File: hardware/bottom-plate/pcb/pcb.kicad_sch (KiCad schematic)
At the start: 27 parts, among them U1 Pico

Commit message: bottom plate schematic, and removed some random stuff
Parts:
- removed DMUX1: TCA9555PWR, Package_SO:TSSOP-24_4.4x7.8mm_P0.65mm, symbol Interface_Expansion:TCA9535PWR
- removed KICK_PWR1: XT30-F, Connector_AMASS:AMASS_XT30U-F_1x02_P5.0mm_Vertical, symbol Connector_Generic:Conn_01x02
- removed PWR1: XT60-M, Connector_AMASS:AMASS_XT60-M_1x02_P7.20mm_Vertical, symbol Connector_Generic:Conn_01x02
- added CTRL1, LOADCELL1: Conn_01x04, Connector_JST:JST_XH_B4B-XH-A_1x04_P2.50mm_Vertical, symbol Connector_Generic:Conn_01x04
- added DMUX1, DMUX2: MCP23S17_SO, Package_SO:SOIC-28W_7.5x17.9mm_P1.27mm, symbol Interface_Expansion:MCP23S17_SO
- added J1: Conn_01x03, symbol Connector_Generic:Conn_01x03
- added KICK1: Conn_01x03, Connector_JST:JST_XH_B3B-XH-A_1x03_P2.50mm_Vertical, symbol Connector_Generic:Conn_01x03
- added R59: 2.7K, PCM_Resistor_SMD_AKL:R_0603_1608Metric_Pad0.98x0.95mm_HandSolder, symbol Device:R
- added R62, R63, R65: DNP, PCM_Resistor_SMD_AKL:R_0603_1608Metric_Pad0.98x0.95mm_HandSolder, symbol Device:R
- added R64, R66: 0R, PCM_Resistor_SMD_AKL:R_0603_1608Metric_Pad0.98x0.95mm_HandSolder, symbol Device:R
- ADC1, ADC2: footprint Package_SO:VSSOP-10_3x3mm_P0.5mm -> Package_SO:TSSOP-10_3x3mm_P0.5mm
- R60: value 4.7K -> 2.7K
- R61: value 4.7K -> 0R
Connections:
- net ADC2_AIN1 is gone; now on net DRV5_IPROPI: ADC2.5 (AIN1)
- net +3V3: now also DMUX1.9 (VDD), DMUX2.9 (VDD), J1.3 (Pin_3), LOADCELL1.1 (Pin_1), R59.1, R63.2, R65.2; no longer U1.36 (3V3)
- net ADC_INT1: now also DMUX1.1 (GPB0)
- net ADC_INT2: now also DMUX1.2 (GPB1)
- net DRV1_NFAULT: now also DMUX1.5 (GPB4)
- net DRV1_NSLEEP: now also DMUX2.2 (GPB1)
- net DRV1_OFF: now also DMUX2.1 (GPB0)
- net DRV1_SCS: now also DMUX2.23 (GPA2); no longer U1.21 (GPIO16)
- net DRV2_NFAULT: now also DMUX1.6 (GPB5)
- net DRV2_NSLEEP: now also DMUX2.4 (GPB3)
- net DRV2_OFF: now also DMUX2.3 (GPB2)
- net DRV2_SCS: now also DMUX2.24 (GPA3)
- net DRV3_NFAULT: now also DMUX1.7 (GPB6)
- net DRV3_NSLEEP: now also DMUX2.6 (GPB5)
- net DRV3_OFF: now also DMUX2.5 (GPB4)
- net DRV3_SCS: now also DMUX2.25 (GPA4)
- net DRV4_NFAULT: now also DMUX1.8 (GPB7)
- net DRV4_NSLEEP: now also DMUX2.8 (GPB7)
- net DRV4_OFF: now also DMUX2.7 (GPB6)
- net DRV4_SCS: now also DMUX2.26 (GPA5)
- net DRV5_IN1: now also U1.19 (GPIO14); no longer U1.25 (GPIO19)
- net DRV5_IN2: now also U1.20 (GPIO15); no longer U1.24 (GPIO18)
- net DRV5_IPROPI: no longer ADC1.7 (AIN3)
- net DRV5_NFAULT: now also DMUX1.21 (GPA0)
- net DRV5_NSLEEP: now also DMUX2.22 (GPA1)
- net DRV5_OFF: now also DMUX2.21 (GPA0)
- net DRV5_SCS: now also DMUX2.27 (GPA6)
- net GND: now also DMUX1.10 (VSS), DMUX2.10 (VSS), J1.2 (Pin_2), KICK1.1 (Pin_1), LOADCELL1.4 (Pin_4), R62.2, R64.1, R66.1
- net LOADCELL_A+: now also LOADCELL1.2 (Pin_2)
- net LOADCELL_A-: now also LOADCELL1.3 (Pin_3)
- net MOUSE1_MOT: now also DMUX1.3 (GPB2)
- net MOUSE1_RST: now also DMUX1.23 (GPA2)
- net MOUSE2_MOT: now also DMUX1.4 (GPB3)
- net MOUSE2_RST: now also DMUX1.24 (GPA3)
- net MUX_S0: now also DMUX1.25 (GPA4); no longer U1.19 (GPIO14)
- net MUX_S1: now also DMUX1.26 (GPA5); no longer U1.20 (GPIO15)
- net MUX_S2: now also DMUX1.27 (GPA6); no longer U1.27 (GPIO21)
- net MUX_S3: now also DMUX1.28 (GPA7); no longer U1.26 (GPIO20)
- net RUN: now also CTRL1.1 (Pin_1)
- net EN: now reaches U1.37 (3V3_EN)
- net EN: now also CTRL1.2 (Pin_2)
- net +5V: now reaches U1.39 (VSYS)
- net at R53.1, R54.2: now also DMUX1.15 (A0)
- net at R55.1, R56.2: now also DMUX1.16 (A1)
- net at R57.1, R58.2: now also DMUX1.17 (A2)
- net +12V renamed VCC
- net VCC: now also KICK1.2 (Pin_2)
- net DMUX_INT renamed RX0
- net RX0: now also CTRL1.3 (Pin_3)
- net MISO renamed SPI0.MISO
- net SPI0.MISO: now also DMUX1.14 (SO), DMUX2.14 (SO)
- net MOSI renamed SPI0.MOSI
- net SPI0.MOSI: now also DMUX1.13 (SI), DMUX2.13 (SI)
- net MUX1_COM renamed AMUX1_COM
- net MUX2_COM renamed AMUX2_COM
- net MUX3_COM renamed AMUX3_COM
- net SCL renamed I2C0.SCL
- net I2C0.SCL: now also R60.2; no longer R61.2
- net SCLK renamed SPI0.SCLK
- net SPI0.SCLK: now also DMUX1.12 (SCK), DMUX2.12 (SCK)
- net SDA renamed I2C0.SDA
- net I2C0.SDA: now also R59.2; no longer R60.2
- new net: DMUX2.17 (A2), R65.1, R66.2
- new net: DMUX2.16 (A1), R63.1, R64.2
- new net: DMUX2.15 (A0), R61.2, R62.1
- new net AMUX_EN: DMUX2.28 (GPA7)
- new net DMUX1_INT: DMUX1.20 (INTA), U1.25 (GPIO19)
- new net DMUX2_INT: DMUX1.22 (GPA1), DMUX2.20 (INTA)
- new net DMUX_RESET: DMUX1.18 (~{RESET}), DMUX2.18 (~{RESET}), U1.26 (GPIO20)
- new net DMUX_SCS: DMUX1.11 (~{CS}), DMUX2.11 (~{CS}), U1.27 (GPIO21)
- new net GATE: ADC1.7 (AIN3), J1.1 (Pin_1)
- new net KICK: KICK1.3 (Pin_3), U1.24 (GPIO18)
- new net TX0: CTRL1.4 (Pin_4), U1.21 (GPIO16)
- no-connect marks 22 -> 29
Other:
- added sheet power (power.kicad_sch)
- note added: "SPI address: 0b0100000"
- note added: "SPI address: 0b0100001"
- note added: "pullup resistors for I2C. Adjust values accordingly. 2.7K is probably safe. lower values can be used if capacitance is too high (shouldnt be the case though since its only on board)"
- note removed: "an xt30 has sufficient current for this. but no point (since batt has xt60 as well.)"
- note removed: "pullup resistors for I2C. Adjust values accordingly. 4.7K is probably a safe value."
- note removed: "this might be headers instead. depends on how kicker PCB is mounted"
- moved on the sheet: DRV1, DRV2, DRV3, DRV4, DRV5, MOUSE_FPC1, MOUSE_FPC2, R53, R54, R55, R56, R57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

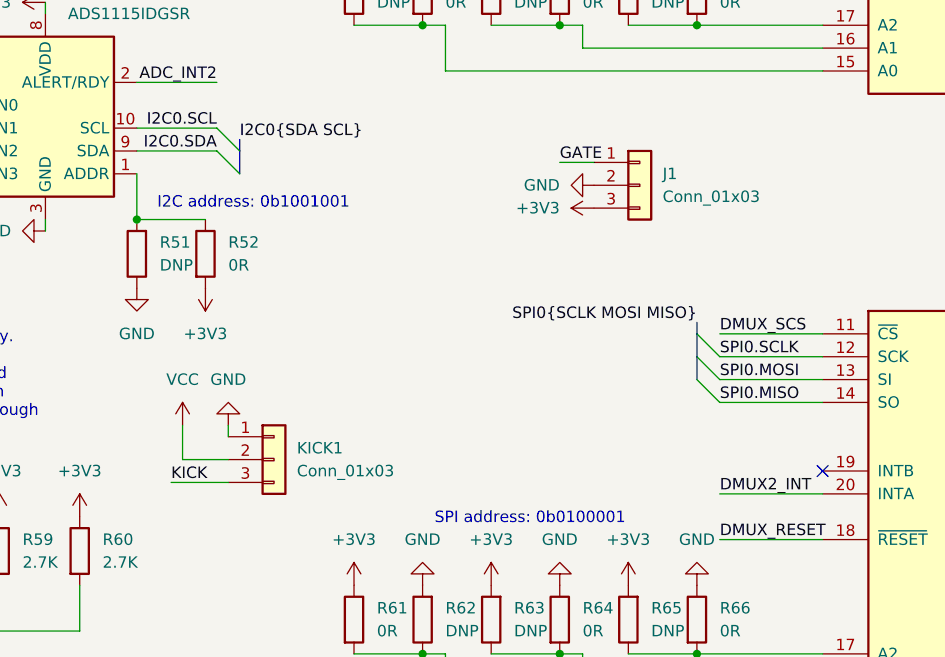
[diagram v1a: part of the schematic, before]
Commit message: kicker pcb done, working on bottom plate
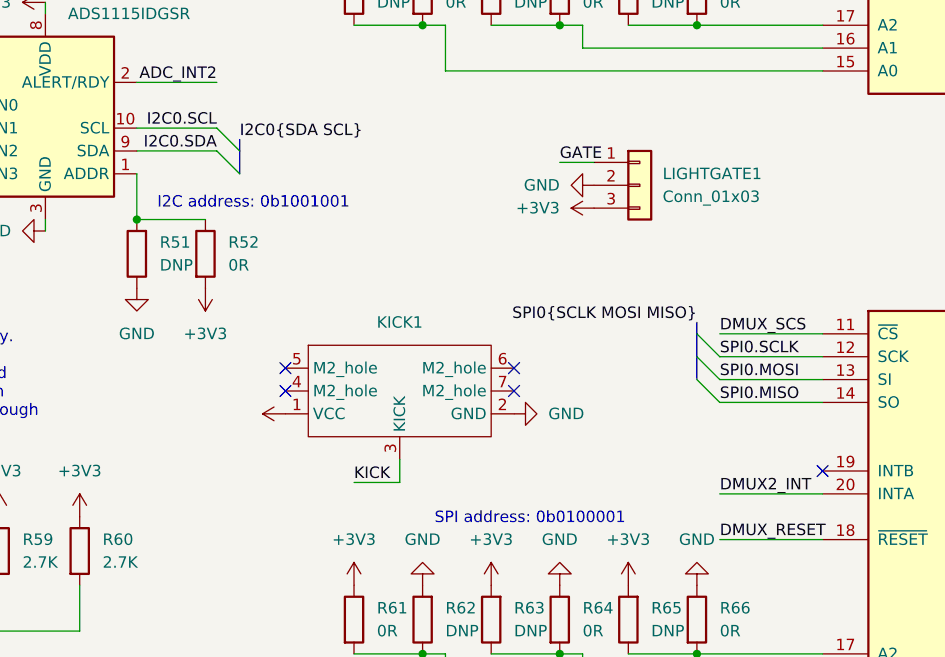
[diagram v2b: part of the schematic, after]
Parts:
- removed KICK1: Conn_01x03, Connector_JST:JST_XH_B3B-XH-A_1x03_P2.50mm_Vertical, symbol Connector_Generic:Conn_01x03
- added KICK1: ~, custom:kicker, symbol custom:kicker
- LIGHTGATE1: renamed from J1; footprint (none) -> Connector_JST:JST_XH_B3B-XH-A_1x03_P2.50mm_Vertical
- R49, R50, R51, R52, R53, R54, R55, R56, R57, R58, R59, R60, R61, R62, R63, R64, R65, R66: footprint PCM_Resistor_SMD_AKL:R_0603_1608Metric_Pad0.98x0.95mm_HandSolder -> PCM_Resistor_SMD_AKL:R_0805_2012Metric_Pad1.15x1.40mm_HandSolder
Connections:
- net GND: now also KICK1.2 (GND)
- net KICK: now also KICK1.3 (KICK)
- net VCC: now also KICK1.1 (VCC)
- no-connect marks 29 -> 33

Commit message: cleaned up bottom plate schematic and added explanations of design decisions. Please read.
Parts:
- added BUCK1: ~, custom:mini560, symbol custom:mini360/560
- added C1: 150uF, Capacitor_SMD:CP_Elec_6.3x7.7, symbol Device:C
- added C2: 1uF, PCM_Capacitor_SMD_AKL:C_0805_2012Metric_Pad1.15x1.40mm_HandSolder, symbol Device:C
- added C3: 22uF, PCM_Capacitor_SMD_AKL:C_0805_2012Metric_Pad1.15x1.40mm_HandSolder, symbol Device:C
- added C4: 10uF, PCM_Capacitor_SMD_AKL:C_0805_2012Metric_Pad1.15x1.40mm_HandSolder, symbol Device:C
- added GATE_LED1: Conn_01x02, Connector_JST:JST_XH_B2B-XH-A_1x02_P2.50mm_Vertical, symbol Connector_Generic:Conn_01x02
- added LDO1: TLV1117-33, Package_TO_SOT_SMD:SOT-223-3_TabPin2, symbol Regulator_Linear:TLV1117-33
- added PWR1: XT60-M, Connector_AMASS:AMASS_XT60-M_1x02_P7.20mm_Vertical, symbol Connector_Generic:Conn_01x02
- added PWR2: XT30-F, Connector_AMASS:AMASS_XT30U-F_1x02_P5.0mm_Vertical, symbol Connector_Generic:Conn_01x02
- U1: footprint RP-Pico Libraries:RPi_Pico_SMD_TH -> RP-Pico Libraries:RPi_Pico_SMD_TH_USBC_cable_cutout
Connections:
- net +3V3: now also C4.2, LDO1.2 (VO)
- net +5V: now also BUCK1.3 (OUT+), C2.2, GATE_LED1.1 (Pin_1), LDO1.3 (VI)
- net ADC_INT1: now also DMUX2.6 (GPB5); no longer DMUX1.1 (GPB0)
- net ADC_INT2: now also DMUX2.7 (GPB6); no longer DMUX1.2 (GPB1)
- net DMUX2_INT: now also DMUX2.8 (GPB7); no longer DMUX1.22 (GPA1)
- net DRV1_NFAULT: now also DMUX2.1 (GPB0); no longer DMUX1.5 (GPB4)
- net DRV1_NSLEEP: now also DMUX1.2 (GPB1); no longer DMUX2.2 (GPB1)
- net DRV1_OFF: now also DMUX1.1 (GPB0); no longer DMUX2.1 (GPB0)
- net DRV1_SCS: now also DMUX2.21 (GPA0); no longer DMUX2.23 (GPA2)
- net DRV2_NFAULT: now also DMUX2.2 (GPB1); no longer DMUX1.6 (GPB5)
- net DRV2_NSLEEP: now also DMUX1.4 (GPB3); no longer DMUX2.4 (GPB3)
- net DRV2_OFF: now also DMUX1.3 (GPB2); no longer DMUX2.3 (GPB2)
- net DRV2_SCS: now also DMUX2.22 (GPA1); no longer DMUX2.24 (GPA3)
- net DRV3_NFAULT: now also DMUX2.3 (GPB2); no longer DMUX1.7 (GPB6)
- net DRV3_NSLEEP: now also DMUX1.6 (GPB5); no longer DMUX2.6 (GPB5)
- net DRV3_OFF: now also DMUX1.5 (GPB4); no longer DMUX2.5 (GPB4)
- net DRV3_SCS: now also DMUX2.23 (GPA2); no longer DMUX2.25 (GPA4)
- net DRV4_NFAULT: now also DMUX2.4 (GPB3); no longer DMUX1.8 (GPB7)
- net DRV4_NSLEEP: now also DMUX1.8 (GPB7); no longer DMUX2.8 (GPB7)
- net DRV4_OFF: now also DMUX1.7 (GPB6); no longer DMUX2.7 (GPB6)
- net DRV4_SCS: now also DMUX2.24 (GPA3); no longer DMUX2.26 (GPA5)
- net DRV5_NFAULT: now also DMUX2.5 (GPB4); no longer DMUX1.21 (GPA0)
- net DRV5_NSLEEP: now also DMUX2.27 (GPA6); no longer DMUX2.22 (GPA1)
- net DRV5_OFF: now also DMUX2.26 (GPA5); no longer DMUX2.21 (GPA0)
- net DRV5_SCS: now also DMUX2.25 (GPA4); no longer DMUX2.27 (GPA6)
- net GND: now also BUCK1.2 (IN-), BUCK1.4 (OUT-), C1.1, C3.1, GATE_LED1.2 (Pin_2), LDO1.1 (GND), PWR1.1 (Pin_1), PWR2.1 (Pin_1)
- net MOUSE1_MOT: now also U1.29 (GPIO22); no longer DMUX1.3 (GPB2)
- net MOUSE1_SCS: now also DMUX1.21 (GPA0); no longer U1.29 (GPIO22)
- net MOUSE2_MOT: now also U1.7 (GPIO5); no longer DMUX1.4 (GPB3)
- net MOUSE2_SCS: now also DMUX1.22 (GPA1); no longer U1.7 (GPIO5)
- net VCC: now also BUCK1.1 (IN+), C1.2, PWR1.2 (Pin_2), PWR2.2 (Pin_2)
- net MUX_S0 renamed AMUX_S0
- net MUX_S1 renamed AMUX_S1
- net MUX_S2 renamed AMUX_S2
- net MUX_S3 renamed AMUX_S3
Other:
- removed sheet line sensors
- removed sheet power
- added sheet line sensor array 1 (line-sensor-array.kicad_sch)
- added sheet line sensor array 2 (line-sensor-array.kicad_sch)
- added sheet line sensor array 3 (line-sensor-array.kicad_sch)
- note added: "16 per array through an analog multiplexer. 48 in total. ALS-PT19 ambient light sensors with HL-PSC-2012H233W(6000-7000K) LEDs shared decoder selection pins, to 3 channels on RP2040"
- note added: "A Pico is used for interfacing the bottom hardware. Connects via UART and USB to the main controller. Pico used for reliable performance and simple implementation with minimal quirks. A USB type-C pico will be preferably used as I hate microusb. Footprint should work fine with both though."
- note added: "ADCs"
- note added: "DRV8244 motor driver breakouts. Output is an XT30. Configured through SPI. Driven via PWM through IN1 and IN2. Current can be read using IPROPI. Read datasheet for more details. DRV5 is for dribbler. A BE-3561 or another brushed motor will be used."
- note added: "Input power smoothing. 150uF should critically damp enough inductance."
- note added: "Lightgate to know if ball is in ball-capture zone. Use of wires to allow different mounting."
- note added: "Loadcell sensor. Can be used in mounting of dribbler suspension to know how well ball is contacting the dribbler. If not using a loadcell, can be used for other analog applications."
- note added: "MINI560 reg, to have a (mostly) guarenteed-to-work and replacable-if-fried design. 5A is way overkill, but the 3A ones are quite sketchy."
- note added: "PMW3360 mouse sensor breakouts, self designed. Uses 1mm pitch FFC connectors. FFC connectors are under this plate for shielding and convenience. 1.6mm thick breakouts has a bit too little ground clearance. Still workable though."
- note added: "Power to middle (and then top) plate. Why not splice wires? It's messy and I don't want to."
- note added: "Reading some sensors, plus monitoring motor currents. Lightgate and loadcell should be on seperate ADCs to minimise contention (especially of the interrupt). Motor currents need not be monitored, but would be cool. Loadcell might not be used due to mass limitations."
- note added: "So the rest of the design can be simpler. And there is only one UART channel on Pi, so only one low-latency microcontroller can exist, unless UART addressing is used, which adds overhead and shares the already limited bandwidth due to running close to many rapidly switching currents. Also, to take up as much bottom real estate as possible, so things don't need to block the camera. And also becaus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"
- note added: "UART channel for low-bandwidth, highly latency sensitive communication between bottom plate and main controller. Also as a backup if USB latencies somehow end up being too high, The bottom plate is more latency sensitive due to it controlling all the movements of the bot."
- note added: "Why so many? Because I don't want to hardwire most configuration pins / have them be set by a jumper. And that there aren't nearly enough pins on the pico. Interrupts also run through here, as there are insuffient pins on the pico. A second microcontroller can be used, but adds unnecessary software complexity when digital multiplexers work fine. 10MHz SPI digital multiplexers are used to be fast 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"
- note added: "an xt30 has sufficient current for this. but no point (since batt has xt60 as well.)"
- note added: "control"
- note added: "digital multiplexers"
- note added: "kicker"
- note added: "line sensor arrays"
- note added: "motor drivers"
- note added: "mouse sensors"
- note added: "pullup resistors for I2C. Internal pullups of the RP2040 might be too weak to reliably drive 400kHz I2C. Adjust values accordingly, 2.7K is probably safe. lower values can be used if capacitance is too high. And of course, no running I2C on wires."
- note added: "why so much stuff on the bottom plate?"
- note removed: "pullup resistors for I2C. Adjust values accordingly. 2.7K is probably safe. lower values can be used if capacitance is too high (shouldnt be the case though since its only on board)"
- moved on the sheet: ADC1, ADC2, CTRL1, DMUX1, DMUX2, DRV1, DRV2, DRV3, DRV4, DRV5, KICK1, LIGHTGATE1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

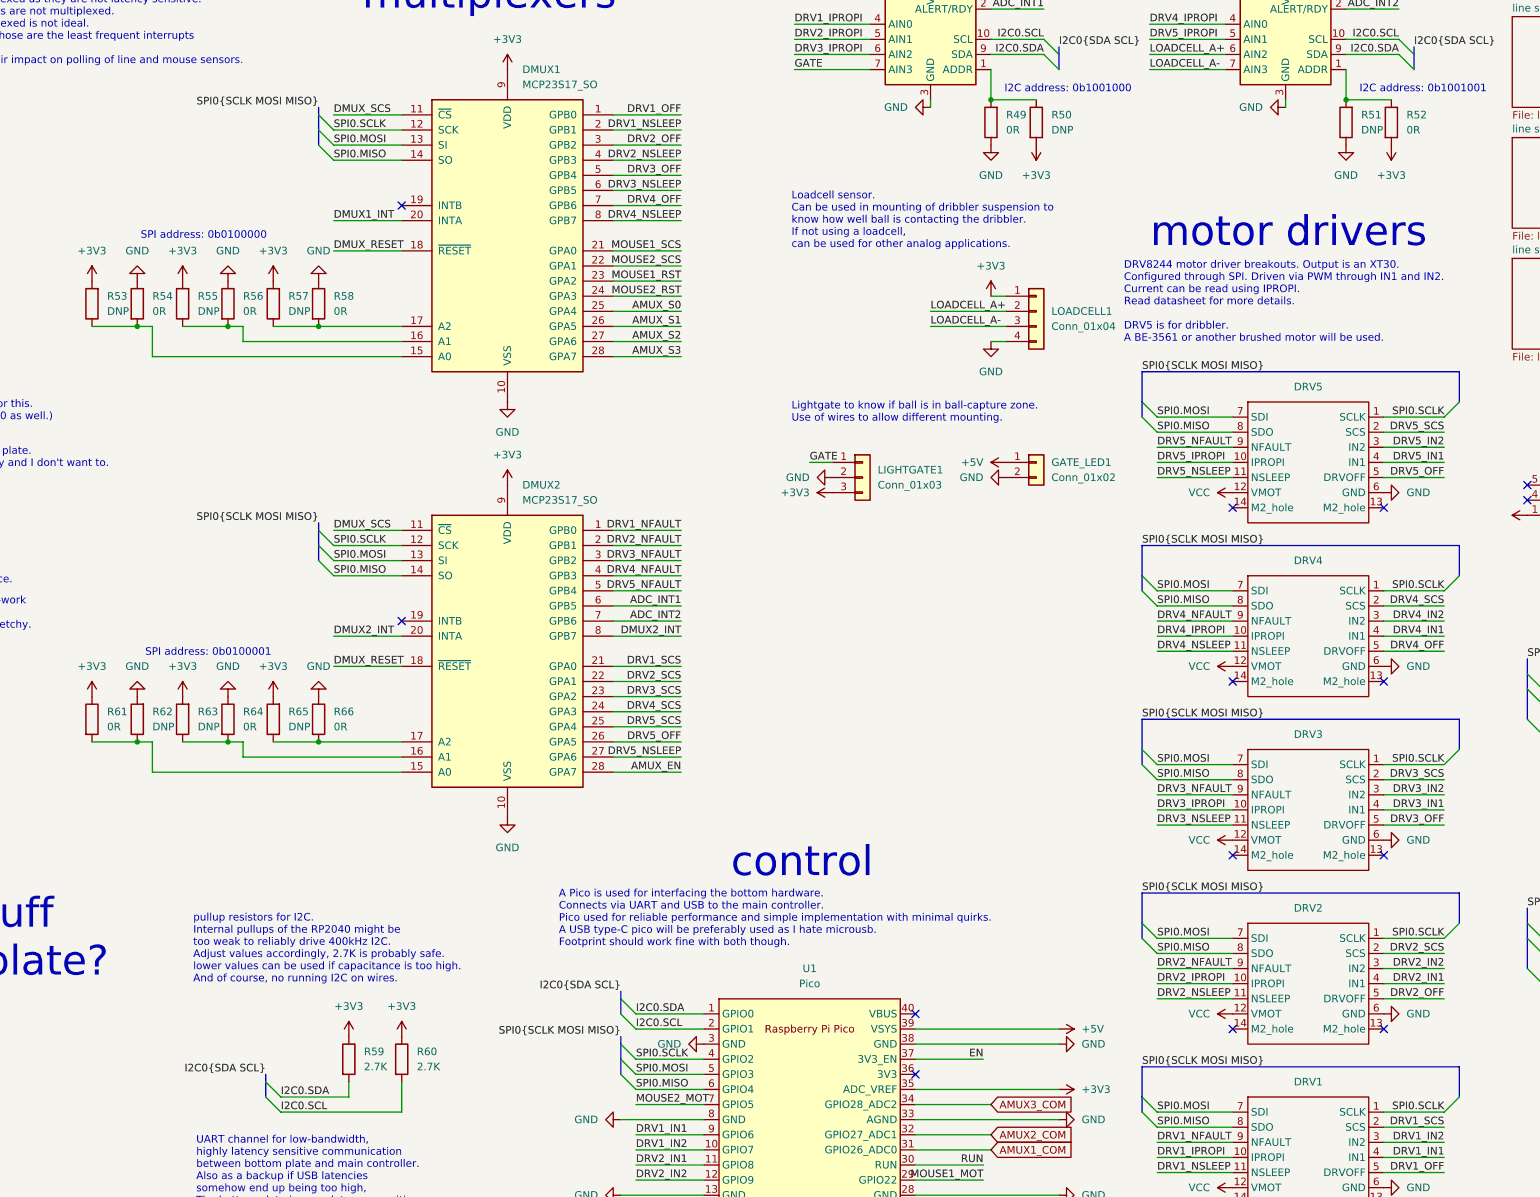
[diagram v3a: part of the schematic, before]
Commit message: cleaned up bottom plate schematic numbering
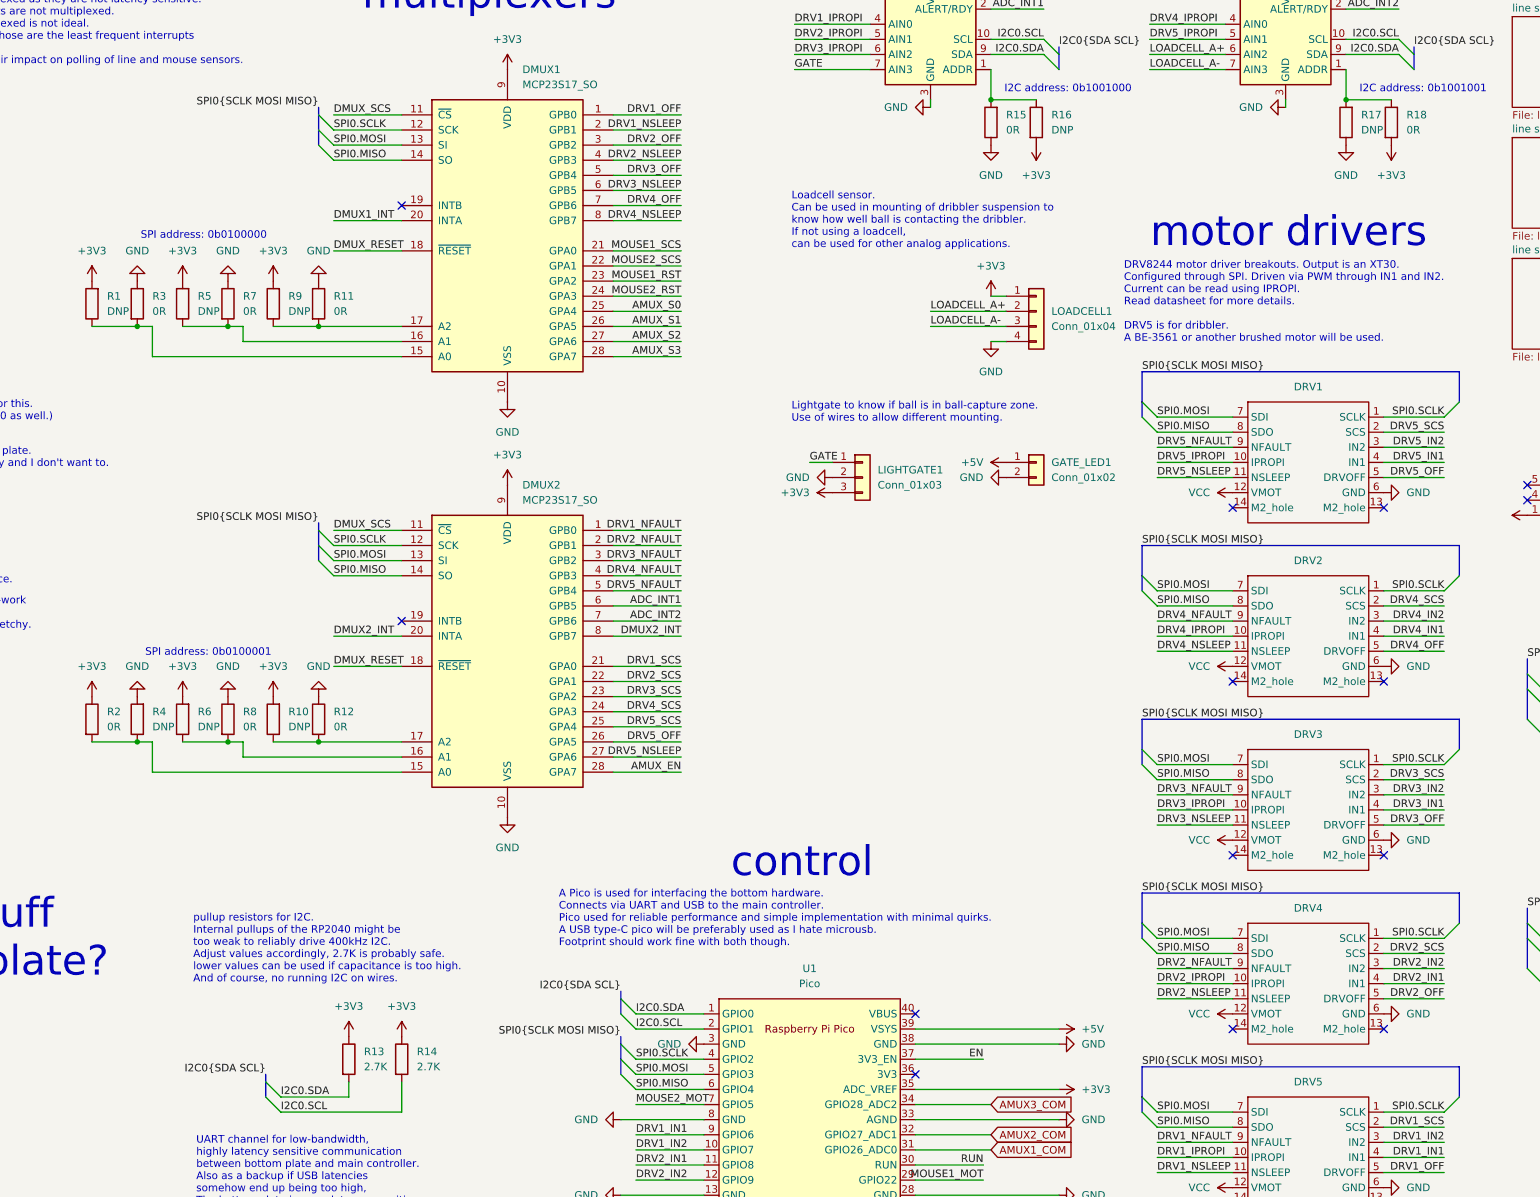
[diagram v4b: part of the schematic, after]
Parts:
- renumbered DRV5 to DRV1, DRV4 to DRV2, DRV2 to DRV4, DRV1 to DRV5, R53 to R1, R65 to R10, R58 to R11, R66 to R12, R59 to R13, R60 to R14, R49 to R15, R50 to R16, R51 to R17, R52 to R18, R61 to R2, R54 to R3, R62 to R4, R55 to R5, R63 to R6, R56 to R7, R64 to R8, R57 to R9
